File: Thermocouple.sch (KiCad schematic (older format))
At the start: 22 parts, among them P2 CONN_3X2, P3 CONN_2, U2 MCP3901, U3 LMT84, U4 OPA4170

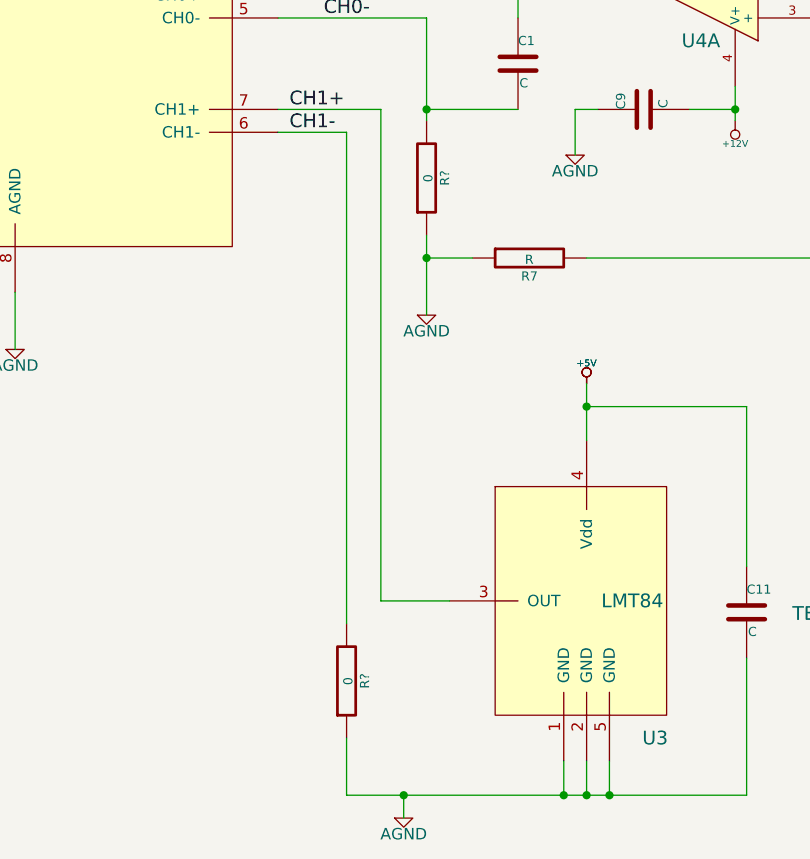
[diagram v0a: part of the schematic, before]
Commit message: Associating the Terminal Blocks
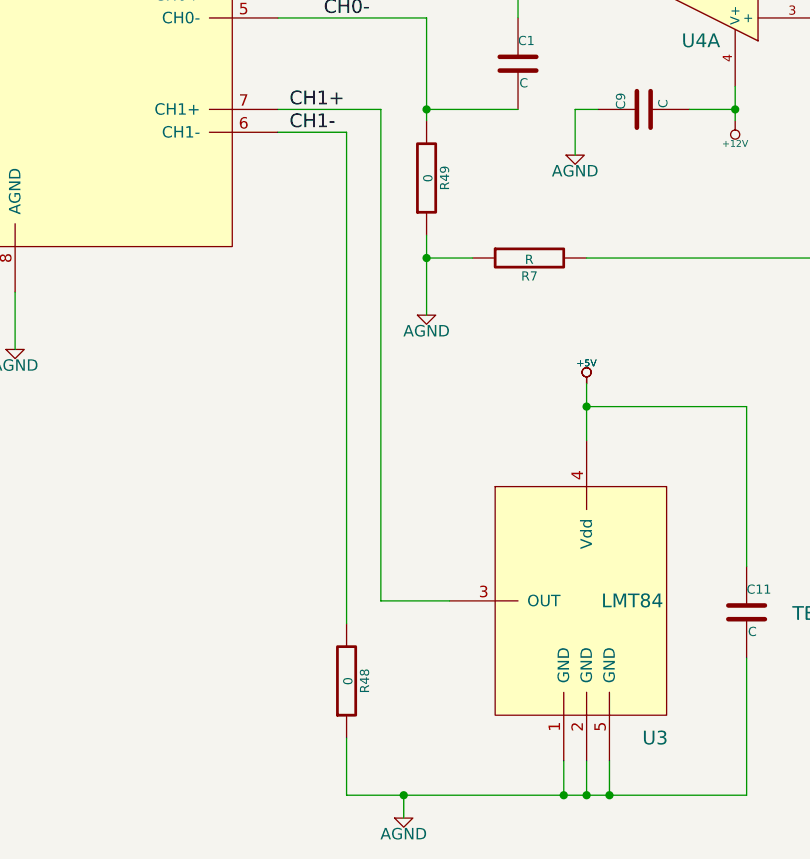
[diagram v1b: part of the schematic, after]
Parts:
- gave numbers to parts that had none: 2
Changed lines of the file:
@@
-EESchema Schematic File Version 2  date 10/11/2013 1:15:54 AM
+EESchema Schematic File Version 2  date 10/11/2013 8:50:27 PM
 LIBS:power
 LIBS:device
@@
 Sheet 2 9
 Title ""
-Date "11 oct 2013"
+Date "12 oct 2013"
 Rev ""
 Comp ""
@@
 $EndComp
 $Comp
-L -12V #PWR01
+L -12V #PWR13
 U 1 1 523646A5
 P 6250 2550
-F 0 "#PWR01" H 6250 2680 20  0001 C CNN
+F 0 "#PWR13" H 6250 2680 20  0001 C CNN
 F 1 "-12V" H 6250 2650 30  0000 C CNN
 F 2 "" H 6250 2550 60  0000 C CNN
@@
 $EndComp
 $Comp
-L -12V #PWR02
+L -12V #PWR16
 U 1 1 523646B2
 P 9000 2850
-F 0 "#PWR02" H 9000 2980 20  0001 C CNN
+F 0 "#PWR16" H 9000 2980 20  0001 C CNN
 F 1 "-12V" H 9000 2950 30  0000 C CNN
 F 2 "" H 9000 2850 60  0000 C CNN
@@
 $EndComp
 $Comp
-L -12V #PWR03
+L -12V #PWR17
 U 1 1 523646B8
 P 9000 3950
-F 0 "#PWR03" H 9000 4080 20  0001 C CNN
+F 0 "#PWR17" H 9000 4080 20  0001 C CNN
 F 1 "-12V" H 9000 4050 30  0000 C CNN
 F 2 "" H 9000 3950 60  0000 C CNN
@@
 $EndComp
 $Comp
-L +12V #PWR04
+L +12V #PWR14
 U 1 1 5236471D
 P 6250 3850
-F 0 "#PWR04" H 6250 3800 20  0001 C CNN
+F 0 "#PWR14" H 6250 3800 20  0001 C CNN
 F 1 "+12V" H 6250 3950 30  0000 C CNN
 F 2 "" H 6250 3850 60  0000 C CNN
@@
 $EndComp
 $Comp
-L +12V #PWR05
+L +12V #PWR15
 U 1 1 5236474B
 P 9000 1800
-F 0 "#PWR05" H 9000 1750 20  0001 C CNN
+F 0 "#PWR15" H 9000 1750 20  0001 C CNN
 F 1 "+12V" H 9000 1900 30  0000 C CNN
 F 2 "" H 9000 1800 60  0000 C CNN
@@
 $EndComp
 $Comp
-L +12V #PWR06
+L +12V #PWR18
 U 1 1 52364796
 P 9000 5000
-F 0 "#PWR06" H 9000 4950 20  0001 C CNN
+F 0 "#PWR18" H 9000 4950 20  0001 C CNN
 F 1 "+12V" H 9000 5100 30  0000 C CNN
 F 2 "" H 9000 5000 60  0000 C CNN
@@
 	9000 5000 9000 4850
 $Comp
-L AGND #PWR07
+L AGND #PWR8
 U 1 1 52364808
 P 4900 4700
-F 0 "#PWR07" H 4900 4700 40  0001 C CNN
+F 0 "#PWR8" H 4900 4700 40  0001 C CNN
 F 1 "AGND" H 4900 4630 50  0000 C CNN
 F 2 "" H 4900 4700 60  0000 C CNN
@@
 Connection ~ 5600 6800
 $Comp
-L AGND #PWR08
+L AGND #PWR7
 U 1 1 525797B7
 P 4800 6900
-F 0 "#PWR08" H 4800 6900 40  0001 C CNN
+F 0 "#PWR7" H 4800 6900 40  0001 C CNN
 F 1 "AGND" H 4800 6830 50  0000 C CNN
 F 2 "" H 4800 6900 60  0000 C CNN
@@
 Connection ~ 4800 6800
 $Comp
-L +5V #PWR09
+L +5V #PWR11
 U 1 1 5257A1D1
 P 5600 5000
-F 0 "#PWR09" H 5600 5090 20  0001 C CNN
+F 0 "#PWR11" H 5600 5090 20  0001 C CNN
 F 1 "+5V" H 5600 5090 30  0000 C CNN
 F 2 "~" H 5600 5000 60  0000 C CNN
@@
 Connection ~ 6250 3800
 $Comp
-L AGND #PWR010
+L AGND #PWR9
 U 1 1 5257A2EE
 P 5550 4000
-F 0 "#PWR010" H 5550 4000 40  0001 C CNN
+F 0 "#PWR9" H 5550 4000 40  0001 C CNN
 F 1 "AGND" H 5550 3930 50  0000 C CNN
 F 2 "" H 5550 4000 60  0000 C CNN
@@
 $EndComp
 $Comp
-L AGND #PWR011
+L AGND #PWR10
 U 1 1 5257A35E
 P 5600 2800
-F 0 "#PWR011" H 5600 2800 40  0001 C CNN
+F 0 "#PWR10" H 5600 2800 40  0001 C CNN
 F 1 "AGND" H 5600 2730 50  0000 C CNN
 F 2 "" H 5600 2800 60  0000 C CNN
@@
 	6050 3800 6250 3800
 $Comp
-L +5V #PWR012
+L +5V #PWR12
 U 1 1 5257A5A4
 P 5600 5000
-F 0 "#PWR012" H 5600 5090 20  0001 C CNN
+F 0 "#PWR12" H 5600 5090 20  0001 C CNN
 F 1 "+5V" H 5600 5090 30  0000 C CNN
 F 2 "~" H 5600 5000 60  0000 C CNN
@@
 $EndComp
 $Comp
-L +5V #PWR013
+L +5V #PWR4
 U 1 1 5257A5AA
 P 3100 1300
-F 0 "#PWR013" H 3100 1390 20  0001 C CNN
+F 0 "#PWR4" H 3100 1390 20  0001 C CNN
 F 1 "+5V" H 3100 1390 30  0000 C CNN
 F 2 "~" H 3100 1300 60  0000 C CNN
@@
 Connection ~ 3100 1500
 $Comp
-L AGND #PWR014
+L AGND #PWR6
 U 1 1 5257A818
 P 3700 1600
-F 0 "#PWR014" H 3700 1600 40  0001 C CNN
+F 0 "#PWR6" H 3700 1600 40  0001 C CNN
 F 1 "AGND" H 3700 1530 50  0000 C CNN
 F 2 "" H 3700 1600 60  0000 C CNN
@@
 Connection ~ 2400 1550
 $Comp
-L AGND #PWR015
+L AGND #PWR1
 U 1 1 5257A963
 P 1750 1650
-F 0 "#PWR015" H 1750 1650 40  0001 C CNN
+F 0 "#PWR1" H 1750 1650 40  0001 C CNN
 F 1 "AGND" H 1750 1580 50  0000 C CNN
 F 2 "" H 1750 1650 60  0000 C CNN
@@
 	1750 1550 1900 1550
 $Comp
-L AGND #PWR016
+L AGND #PWR2
 U 1 1 5257A9D6
 P 2300 4850
-F 0 "#PWR016" H 2300 4850 40  0001 C CNN
+F 0 "#PWR2" H 2300 4850 40  0001 C CNN
 F 1 "AGND" H 2300 4780 50  0000 C CNN
 F 2 "" H 2300 4850 60  0000 C CNN
@@
 	3100 4600 3100 4850
 $Comp
-L AGND #PWR017
+L AGND #PWR5
 U 1 1 5257AABC
 P 3100 4850
-F 0 "#PWR017" H 3100 4850 40  0001 C CNN
+F 0 "#PWR5" H 3100 4850 40  0001 C CNN
 F 1 "AGND" H 3100 4780 50  0000 C CNN
 F 2 "" H 3100 4850 60  0000 C CNN
@@
 $EndComp
 $Comp
-L +5V #PWR018
+L +5V #PWR3
 U 1 1 5257AAC2
 P 2400 1300
-F 0 "#PWR018" H 2400 1390 20  0001 C CNN
+F 0 "#PWR3" H 2400 1390 20  0001 C CNN
 F 1 "+5V" H 2400 1390 30  0000 C CNN
 F 2 "~" H 2400 1300 60  0000 C CNN
@@
 	4900 3400 4900 3850
 $Comp
-L R R?
+L R R49
 U 1 1 5257936D
 P 4900 4100
-F 0 "R?" V 4980 4100 40  0000 C CNN
+F 0 "R49" V 4980 4100 40  0000 C CNN
 F 1 "0" V 4907 4101 40  0000 C CNN
 F 2 "~" V 4830 4100 30  0000 C CNN
@@
 	4900 4350 4900 4700
 $Comp
-L R R?
+L R R48
 U 1 1 525794CD
 P 4550 6300
-F 0 "R?" V 4630 6300 40  0000 C CNN
+F 0 "R48" V 4630 6300 40  0000 C CNN
 F 1 "0" V 4557 6301 40  0000 C CNN
 F 2 "~" V 4480 6300 30  0000 C CNN
